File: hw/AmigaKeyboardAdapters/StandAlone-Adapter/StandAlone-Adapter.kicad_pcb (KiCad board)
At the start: 2 copper layers, 78.7 x 58.4 mm, 56 parts, among them J1 RJ10, J2 Conn_02x03_Odd_Even, P1 CONN_01X02, Q1 BSS138, Q2 BSS138, Q3 BSS138, U1 AZ1117-3.3, U3 STM32F401RCTx

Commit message: added filled zone and changed footprint for button reset
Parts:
- RESET1: footprint Buttons_Switches_SMD:SW_SPST_FSMSM -> RetroBitLab:SW_SPST_FSMSM_3D
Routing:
- added copper zone on F.Cu, net GND
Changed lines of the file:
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@@
     (links 110)
     (no_connects 0)
-    (area 109.144999 65.964999 188.035001 124.535001)
+    (area 107.921667 58.11 203.58 128.799001)
     (thickness 1.6)
     (drawings 35)
@@
     )
   )
-  (module Buttons_Switches_SMD:SW_SPST_FSMSM (layer F.Cu)
-    (at 114.3 96.52 90)
-    (descr http://www.te.com/commerce/DocumentDelivery/DDEController?Action=srchrtrv&DocNm=1437566-3&DocType=Customer+Drawing&DocLang=English)
-    (tags "SPST button tactile switch")
-    (attr smd)
-    (fp_text reference RESET1 (at 0.01011 -2.60022 90) (layer F.SilkS) hide
-      (effects (font (size 1 1) (thickness 0.15)))
-    )
-    (fp_text value SW_PUSH (at 0.01011 -0.00022 90) (layer F.Fab)
-      (effects (font (size 1 1) (thickness 0.15)))
-    )
-    (fp_line (start -1.23989 -0.55022) (end 1.26011 -0.55022) (layer F.SilkS) (width 0.15))
-    (fp_line (start 1.26011 -0.55022) (end 1.26011 0.54978) (layer F.SilkS) (width 0.15))
-    (fp_line (start 1.26011 0.54978) (end -1.23989 0.54978) (layer F.SilkS) (width 0.15))
-    (fp_line (start -1.23989 0.54978) (end -1.23989 -0.55022) (layer F.SilkS) (width 0.15))
-    (fp_line (start -1.48989 0.79978) (end 1.51011 0.79978) (layer F.SilkS) (width 0.15))
-    (fp_line (start -1.48989 -0.80022) (end 1.51011 -0.80022) (layer F.SilkS) (width 0.15))
-    (fp_line (start 1.51011 -0.80022) (end 1.51011 0.79978) (layer F.SilkS) (width 0.15))
-    (fp_line (start -1.48989 -0.80022) (end -1.48989 0.79978) (layer F.SilkS) (width 0.15))
-    (fp_line (start -5.85 1.95) (end 5.9 1.95) (layer F.CrtYd) (width 0.05))
-    (fp_line (start 5.9 -2) (end 5.9 1.95) (layer F.CrtYd) (width 0.05))
-    (fp_line (start -2.98989 1.74978) (end 3.01011 1.74978) (layer F.SilkS) (width 0.15))
-    (fp_line (start -2.98989 -1.75022) (end 3.01011 -1.75022) (layer F.SilkS) (width 0.15))
-    (fp_line (start -2.98989 -1.75022) (end -2.98989 1.74978) (layer F.SilkS) (width 0.15))
-    (fp_line (start 3.01011 -1.75022) (end 3.01011 1.74978) (layer F.SilkS) (width 0.15))
-    (fp_line (start -5.85 -2) (end -5.85 1.95) (layer F.CrtYd) (width 0.05))
-    (fp_line (start -5.85 -2) (end 5.9 -2) (layer F.CrtYd) (width 0.05))
-    (pad 1 smd rect (at -4.60243 -0.00232 90) (size 2.18 1.6) (layers F.Cu F.Paste F.Mask)
-      (net 16 "Net-(EN1-Pad1)"))
-    (pad 2 smd rect (at 4.60243 0.00232 90) (size 2.18 1.6) (layers F.Cu F.Paste F.Mask)
-      (net 3 GND))
-  )
   (module Resistors_SMD:R_0603_HandSoldering (layer F.Cu)
     (at 124.46 88.9)
@@
     )
   )
+  (module RetroBitLab:SW_SPST_FSMSM_3D (layer F.Cu)
+    (at 114.3 96.52 90)
+    (descr http://www.te.com/commerce/DocumentDelivery/DDEController?Action=srchrtrv&DocNm=1437566-3&DocType=Customer+Drawing&DocLang=English)
+    (tags "SPST button tactile switch")
+    (attr smd)
+    (fp_text reference RESET1 (at 0 -2.6 90) (layer F.SilkS) hide
+      (effects (font (size 1 1) (thickness 0.15)))
+    )
+    (fp_text value SW_PUSH (at 0 3 90) (layer F.Fab)
+      (effects (font (size 1 1) (thickness 0.15)))
+    )
+    (fp_text user %R (at 0 -2.6 90) (layer F.Fab)
+      (effects (font (size 1 1) (thickness 0.15)))
+    )
+    (fp_line (start -1.75 -1) (end 1.75 -1) (layer F.Fab) (width 0.1))
+    (fp_line (start 1.75 -1) (end 1.75 1) (layer F.Fab) (width 0.1))
+    (fp_line (start 1.75 1) (end -1.75 1) (layer F.Fab) (width 0.1))
+    (fp_line (start -1.75 1) (end -1.75 -1) (layer F.Fab) (width 0.1))
+    (fp_line (start -3.06 -1.81) (end 3.06 -1.81) (layer F.SilkS) (width 0.12))
+    (fp_line (start 3.06 -1.81) (end 3.06 1.81) (layer F.SilkS) (width 0.12))
+    (fp_line (start 3.06 1.81) (end -3.06 1.81) (layer F.SilkS) (width 0.12))
+    (fp_line (start -3.06 1.81) (end -3.06 -1.81) (layer F.SilkS) (width 0.12))
+    (fp_line (start -1.5 0.8) (end 1.5 0.8) (layer F.Fab) (width 0.1))
+    (fp_line (start -1.5 -0.8) (end 1.5 -0.8) (layer F.Fab) (width 0.1))
+    (fp_line (start 1.5 -0.8) (end 1.5 0.8) (layer F.Fab) (width 0.1))
+    (fp_line (start -1.5 -0.8) (end -1.5 0.8) (layer F.Fab) (width 0.1))
+    (fp_line (start -5.95 2) (end 5.95 2) (layer F.CrtYd) (width 0.05))
+    (fp_line (start 5.95 -2) (end 5.95 2) (layer F.CrtYd) (width 0.05))
+    (fp_line (start -3 1.75) (end 3 1.75) (layer F.Fab) (width 0.1))
+    (fp_line (start -3 -1.75) (end 3 -1.75) (layer F.Fab) (width 0.1))
+    (fp_line (start -3 -1.75) (end -3 1.75) (layer F.Fab) (width 0.1))
+    (fp_line (start 3 -1.75) (end 3 1.75) (layer F.Fab) (width 0.1))
+    (fp_line (start -5.95 -2) (end -5.95 2) (layer F.CrtYd) (width 0.05))
+    (fp_line (start -5.95 -2) (end 5.95 -2) (layer F.CrtYd) (width 0.05))
+    (pad 1 smd rect (at -4.59 0 90) (size 2.18 1.6) (layers F.Cu F.Paste F.Mask)
+      (net 16 "Net-(EN1-Pad1)"))
+    (pad 2 smd rect (at 4.59 0 90) (size 2.18 1.6) (layers F.Cu F.Paste F.Mask)
+      (net 3 GND))
+    (model /home/debian/packages/kicad/kicad-packages3D/Button_Switch_SMD.3dshapes/SW_SPST_FSMSM.wrl
+      (at (xyz 0 0 0))
+      (scale (xyz 1 1 1))
+      (rotate (xyz 0 0 0))
+    )
+  )
   (gr_circle (center 142.367 94.742) (end 142.494 94.742) (layer F.SilkS) (width 0.2))
   (gr_text "powered by" (at 143.51 82.55) (layer B.SilkS)
@@
       )
     )
+  )
+  (zone (net 3) (net_name GND) (layer F.Cu) (hatch edge 0.508)
+    (connect_pads (clearance 0.508))
+    (min_thickness 0.254)
+    (fill yes (arc_segments 16) (thermal_gap 0.508) (thermal_bridge_width 0.508))
+    (polygon
+      (pts
+        (xy 187.5 124) (xy 109.75 124) (xy 109.75 66.75) (xy 187.5 66.75) (xy 187.5 124)
+      )
+    )

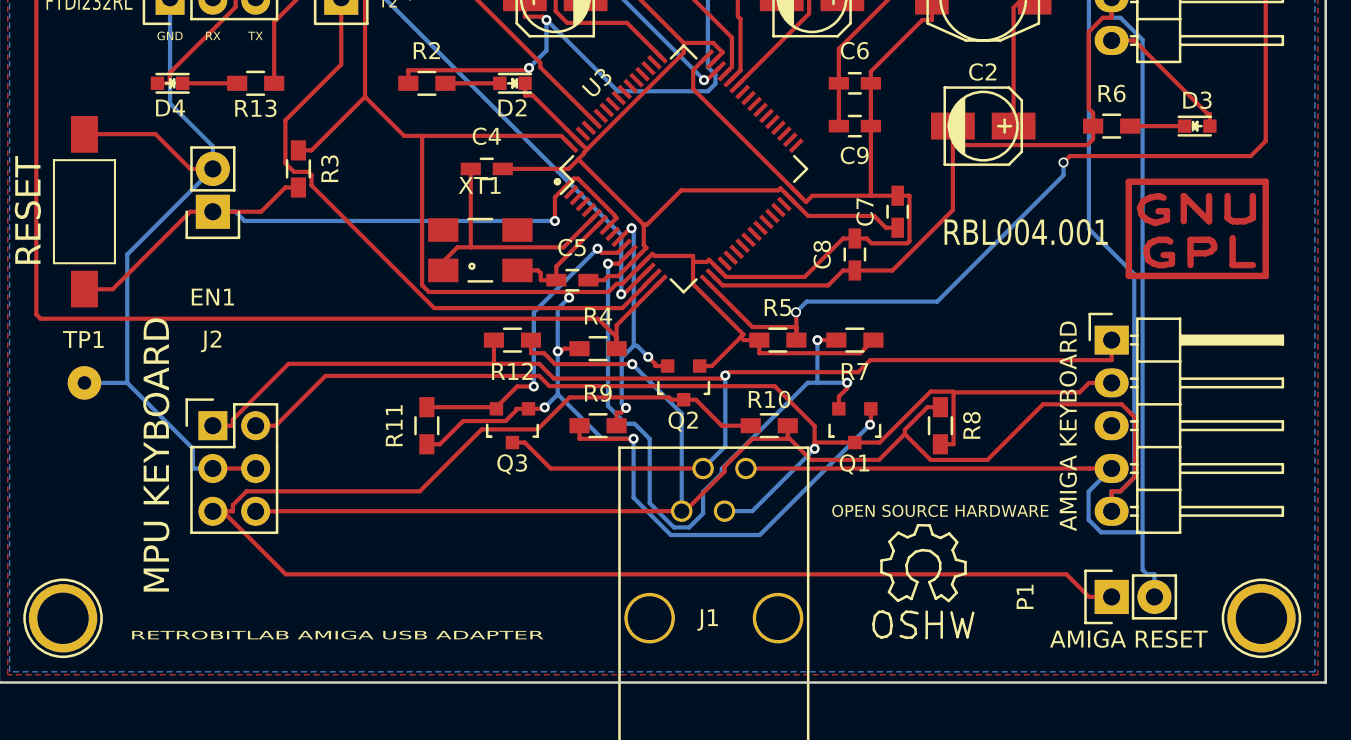
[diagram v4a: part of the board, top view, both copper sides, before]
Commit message: modified for IDC Connector
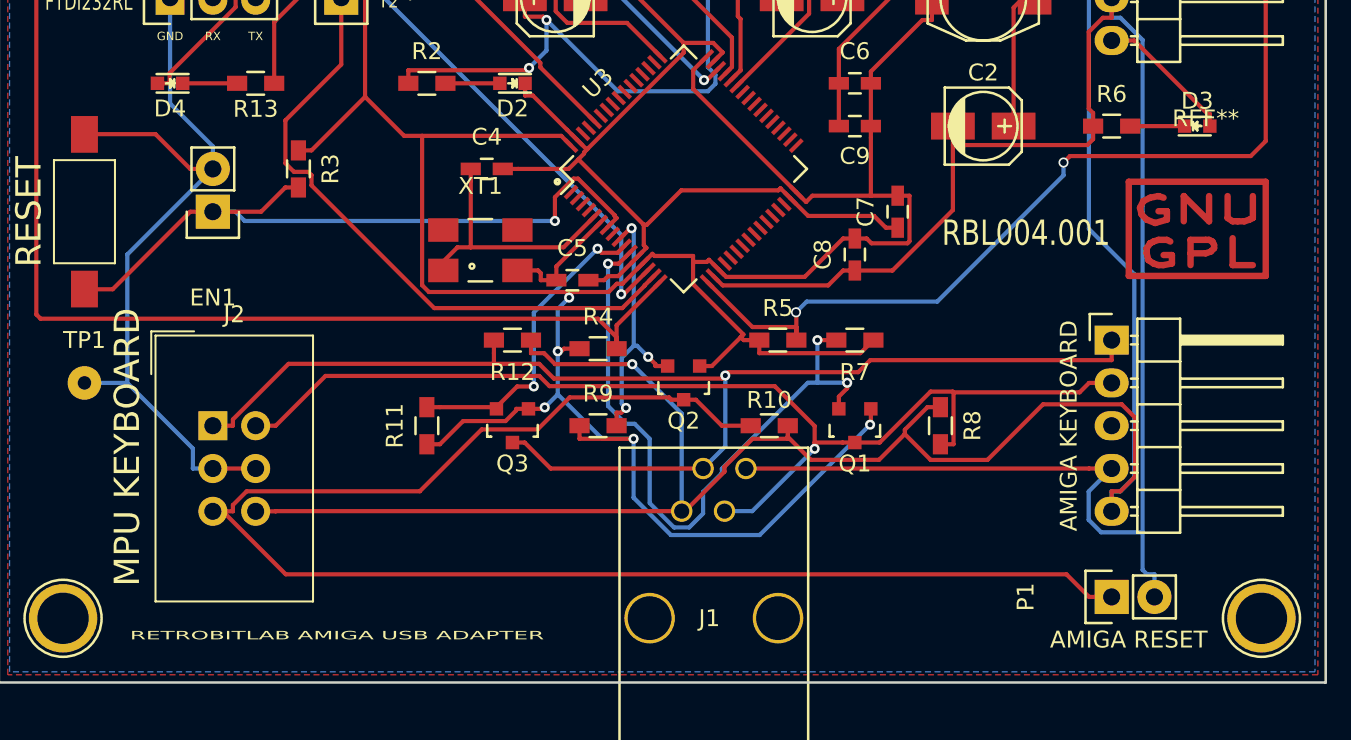
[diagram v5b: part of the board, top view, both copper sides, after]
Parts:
- removed AMIGALOGO: LOGO, RetroBitLab:amigaLogo_BW_31x12mm-SilkScreenBack
- removed GNUGPL: Symbol_GNU-GPL_CopperTop_Small, Symbols:Symbol_GNU-GPL_CopperTop_Small
- removed OPEN SOURCE HARDWARE: Symbol_OSHW-Logo_SilkScreen, Symbols:Symbol_OSHW-Logo_SilkScreen
- removed WORKBENCHLOGO: LOGO, RetroBitLab:amigaWorkBench1-SIlkScreenBack
- added G***: LOGO, RetroBitLab:amigaLogo_BW_31x12mm-SilkScreenBack, B.Cu at (151.1, 86.4)
- added G***: LOGO, RetroBitLab:amigaWorkBench1-SIlkScreenBack, B.Cu at (147.3, 101.6)
- added REF**: Symbol_GNU-GPL_CopperTop_Small, Symbols:Symbol_GNU-GPL_CopperTop_Small, F.Cu at (180.3, 97.8)
- J2: footprint Pin_Headers:Pin_Header_Straight_2x03 -> Connector_IDC:IDC-Header_2x03_P2.54mm_Vertical

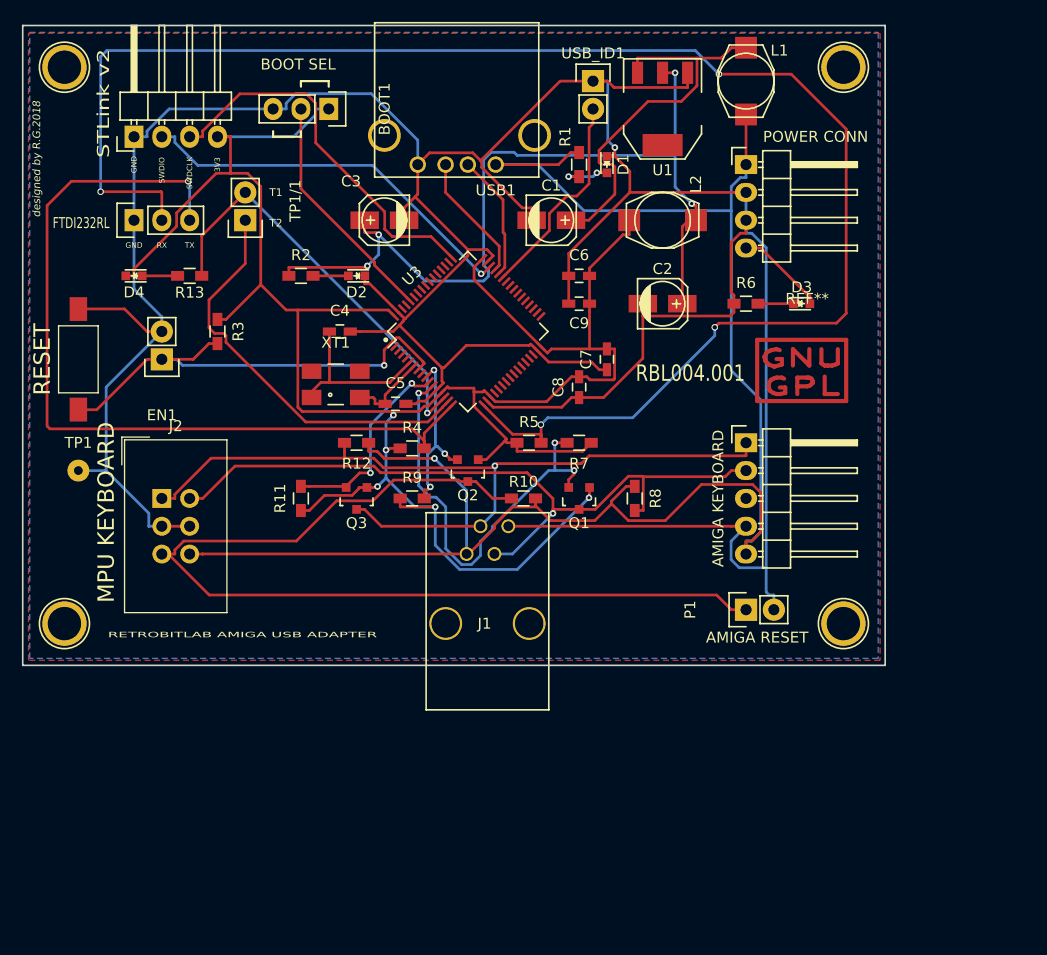
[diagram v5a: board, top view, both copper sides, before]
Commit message: added the idc 2x3 box
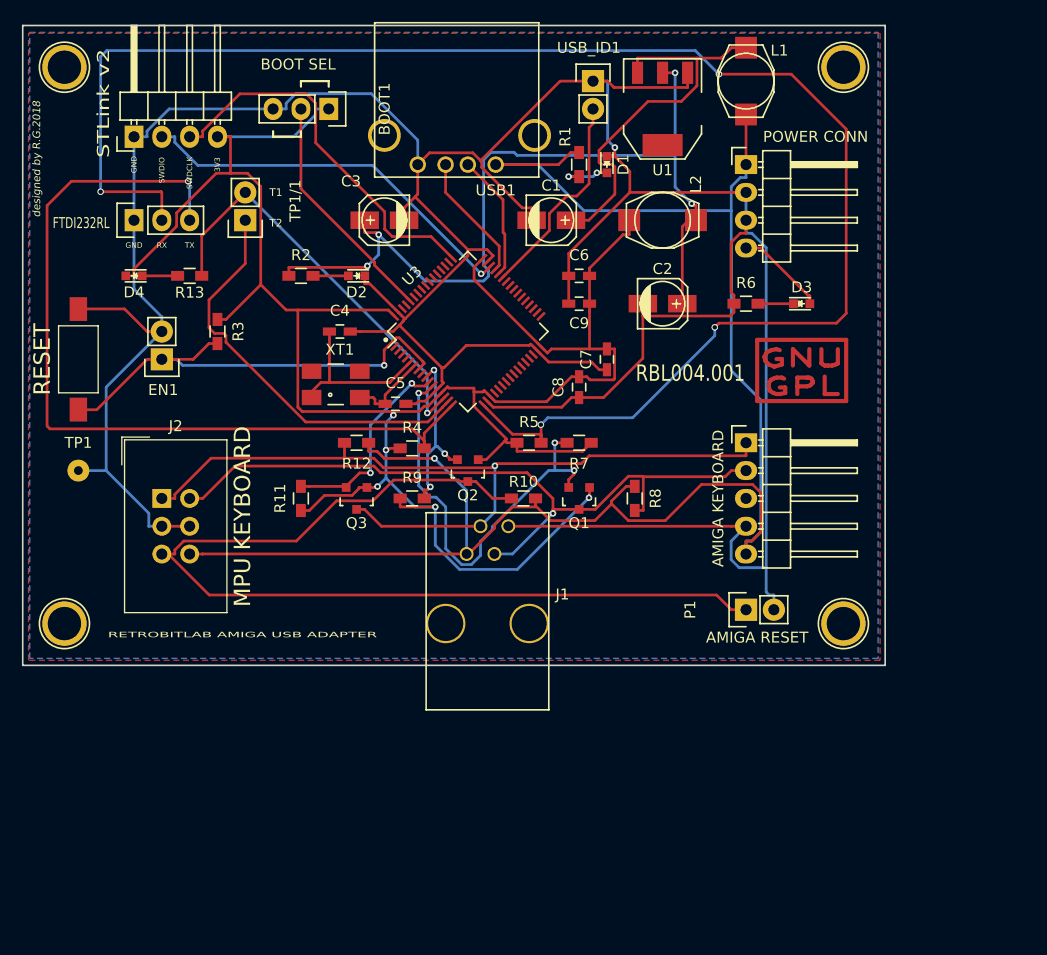
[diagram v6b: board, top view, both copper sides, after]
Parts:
- renumbered REF** to GPLLOGO
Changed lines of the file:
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@@
     (links 110)
     (no_connects 0)
-    (area 109.144999 65.964999 188.035001 124.535001)
+    (area 107.921667 58.11 203.58 128.799001)
     (thickness 1.6)
     (drawings 35)
@@
     (uvia_drill 0.1)
   )
-  (module RetroBitLab:RJ10-RECEPTACLE-Assmann-ASS-2004-3-4-LP-N-R (layer F.Cu)
-    (at 146.05 110.49)
-    (tags "RJ10 4P4C")
-    (fp_text reference J1 (at 5.334 10.16) (layer F.SilkS)
-      (effects (font (size 1 1) (thickness 0.15)))
-    )
-    (fp_text value RJ10 (at 5.842 7.874 180) (layer F.Fab)
-      (effects (font (size 1 1) (thickness 0.15)))
-    )
-    (fp_line (start 0 0.034) (end 11.2 0.034) (layer F.SilkS) (width 0.15))
-    (fp_line (start 11.2 18.034) (end 11.2 0.034) (layer F.SilkS) (width 0.15))
-    (fp_line (start 0 18.034) (end 0 0.034) (layer F.SilkS) (width 0.15))
-    (fp_line (start 0 18.034) (end 11.2 18.034) (layer F.SilkS) (width 0.15))
-    (pad 3 thru_hole circle (at 6.235 3.8) (size 1.27 1.27) (drill 0.9) (layers *.Cu *.Mask F.SilkS)
-      (net 2 KBD_DATA))
-    (pad 1 thru_hole circle (at 3.695 3.8) (size 1.27 1.27) (drill 0.9) (layers *.Cu *.Mask F.SilkS)
-      (net 4 VCC5V))
-    (pad 4 thru_hole circle (at 7.505 1.27) (size 1.27 1.27) (drill 0.9) (layers *.Cu *.Mask F.SilkS)
-      (net 3 GND))
-    (pad 5 thru_hole circle (at 9.41 10.15) (size 3 3) (drill 2.6) (layers *.Cu *.Mask F.SilkS))
-    (pad 5 thru_hole circle (at 1.79 10.15) (size 3 3) (drill 2.6) (layers *.Cu *.Mask F.SilkS))
-    (pad 2 thru_hole circle (at 4.965 1.27) (size 1.27 1.27) (drill 0.9) (layers *.Cu *.Mask F.SilkS)
-      (net 1 KBD_CLOCK))
-  )
   (module Connect:1pin (layer F.Cu)
     (at 113.03 120.65)
@@
     (tags "Crystal, Quarz, SMD, 0603, 4 Pads,")
     (attr smd)
-    (fp_text reference XT1 (at 0 -3.81) (layer F.SilkS)
+    (fp_text reference XT1 (at 0.381 -3.175) (layer F.SilkS)
       (effects (font (size 1 1) (thickness 0.15)))
     )
@@
     (descr "Through hole pin header")
     (tags "pin header")
-    (fp_text reference USB_ID1 (at 0 -2.54) (layer F.SilkS)
+    (fp_text reference USB_ID1 (at -0.381 -3.048) (layer F.SilkS)
       (effects (font (size 1 1) (thickness 0.15)))
     )
@@
     (descr "Through hole pin header")
     (tags "pin header")
-    (fp_text reference EN1 (at 0 -5.1 180) (layer F.SilkS)
+    (fp_text reference EN1 (at -0.127 -2.794 180) (layer F.SilkS)
       (effects (font (size 1 1) (thickness 0.15)))
     )
@@
     (descr "Symbol, GNU-GPL, Copper Top, Small,")
     (tags "Symbol, GNU-GPL, Copper Top, Small,")
-    (fp_text reference REF** (at 0.50038 -6.79958) (layer F.SilkS)
+    (fp_text reference GPLLOGO (at 0.50038 -6.79958) (layer F.SilkS) hide
       (effects (font (size 1 1) (thickness 0.15)))
     )
@@
       (xy -3.894666 9.059333) (xy -3.894688 8.3185)) (layer B.SilkS) (width 0.01))
   )
+  (module RetroBitLab:RJ10-RECEPTACLE-Assmann-ASS-2004-3-4-LP-N-R (layer F.Cu)
+    (at 146.05 110.49)
+    (tags "RJ10 4P4C")
+    (fp_text reference J1 (at 12.446 7.493) (layer F.SilkS)
+      (effects (font (size 1 1) (thickness 0.15)))
+    )
+    (fp_text value RJ10 (at 5.842 7.874 180) (layer F.Fab)
+      (effects (font (size 1 1) (thickness 0.15)))
+    )
+    (fp_line (start 0 0.034) (end 11.2 0.034) (layer F.SilkS) (width 0.15))
+    (fp_line (start 11.2 18.034) (end 11.2 0.034) (layer F.SilkS) (width 0.15))
+    (fp_line (start 0 18.034) (end 0 0.034) (layer F.SilkS) (width 0.15))
+    (fp_line (start 0 18.034) (end 11.2 18.034) (layer F.SilkS) (width 0.15))
+    (pad 3 thru_hole circle (at 6.235 3.8) (size 1.27 1.27) (drill 0.9) (layers *.Cu *.Mask F.SilkS)
+      (net 2 KBD_DATA))
+    (pad 1 thru_hole circle (at 3.695 3.8) (size 1.27 1.27) (drill 0.9) (layers *.Cu *.Mask F.SilkS)
+      (net 4 VCC5V))
+    (pad 4 thru_hole circle (at 7.505 1.27) (size 1.27 1.27) (drill 0.9) (layers *.Cu *.Mask F.SilkS)
+      (net 3 GND))
+    (pad 5 thru_hole circle (at 9.41 10.15) (size 3.6 3.6) (drill 3.2) (layers *.Cu *.Mask F.SilkS))
+    (pad 5 thru_hole circle (at 1.79 10.15) (size 3.6 3.6) (drill 3.2) (layers *.Cu *.Mask F.SilkS))
+    (pad 2 thru_hole circle (at 4.965 1.27) (size 1.27 1.27) (drill 0.9) (layers *.Cu *.Mask F.SilkS)
+      (net 1 KBD_CLOCK))
+  )
   (gr_circle (center 142.367 94.742) (end 142.494 94.742) (layer F.SilkS) (width 0.2))
   (gr_text "powered by" (at 143.51 82.55) (layer B.SilkS)
@@
     (effects (font (size 1.5 1.5) (thickness 0.3)))
   )
-  (gr_text "MPU KEYBOARD " (at 116.84 110.49 90) (layer F.SilkS)
+  (gr_text "MPU KEYBOARD " (at 129.286 110.871 90) (layer F.SilkS)
     (effects (font (size 1.5 1.5) (thickness 0.3)))
   )
